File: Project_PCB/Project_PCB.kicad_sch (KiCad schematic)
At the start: 47 parts, among them J1 USB_C_2.0, J2 Myoware Connector, J3 Conn_01x02, SW1 RESET, SW2 BOOT, SW3 POWER, U1 ESP32-S3-WROOM-1, U2 RT9080-33GJ5, U3 MCP73831T-2ACI/OT, U4 LMV321

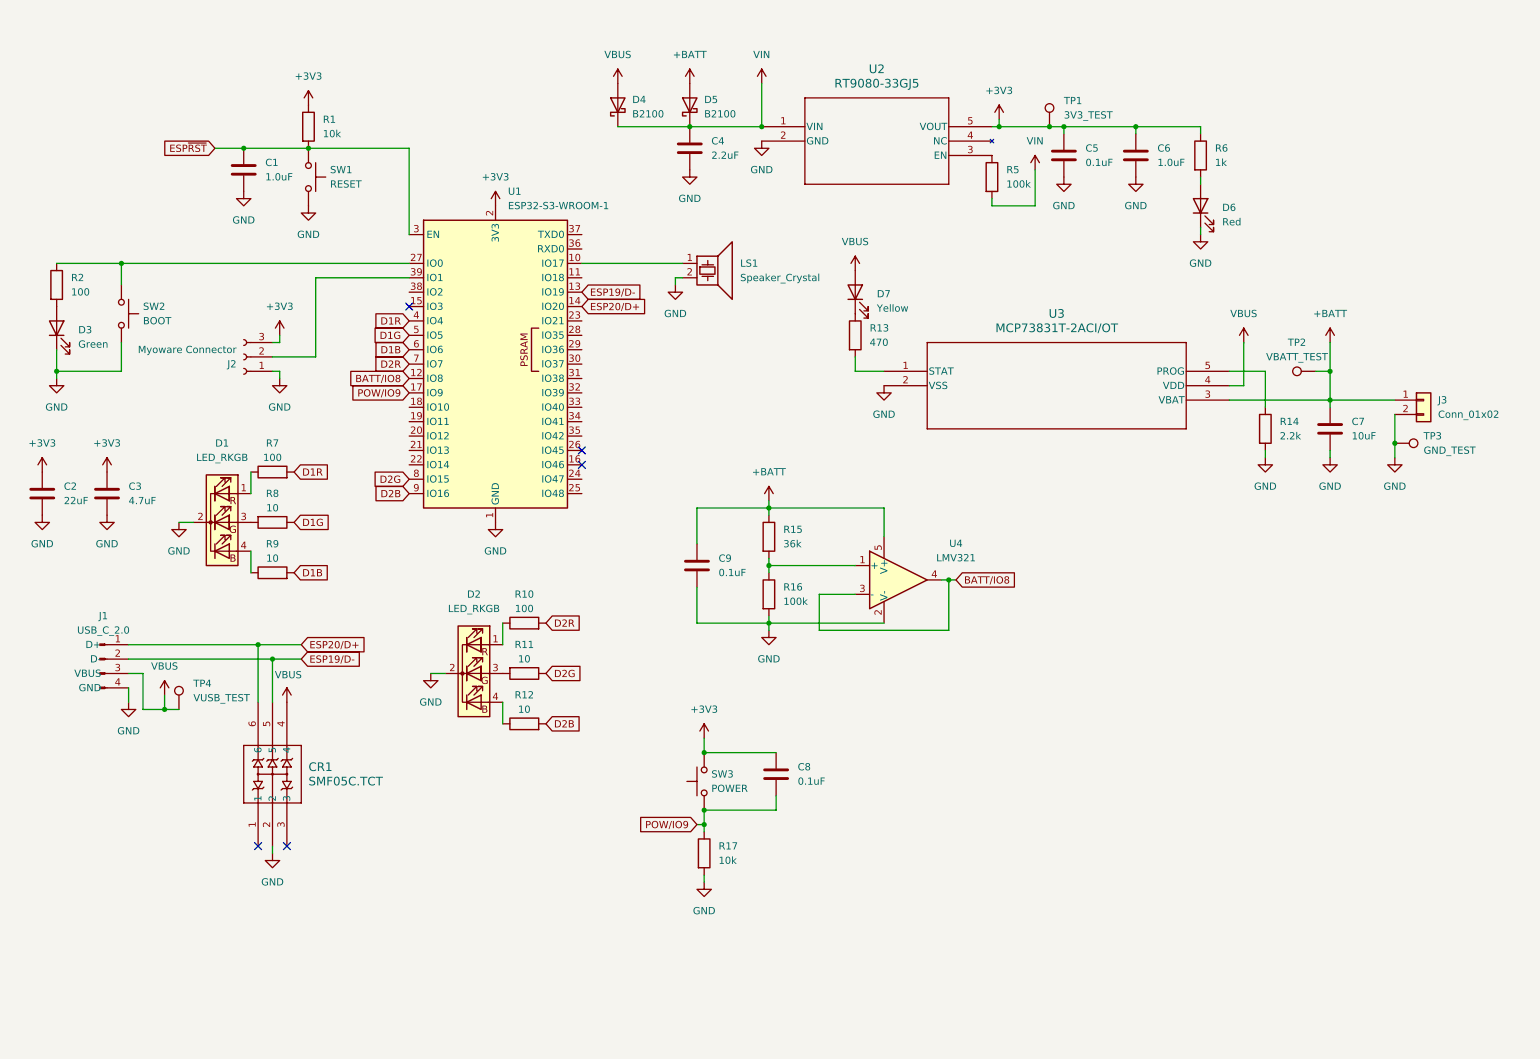
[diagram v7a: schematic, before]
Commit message: Made progress on PCB layout; minor changes in schematic to ease routing
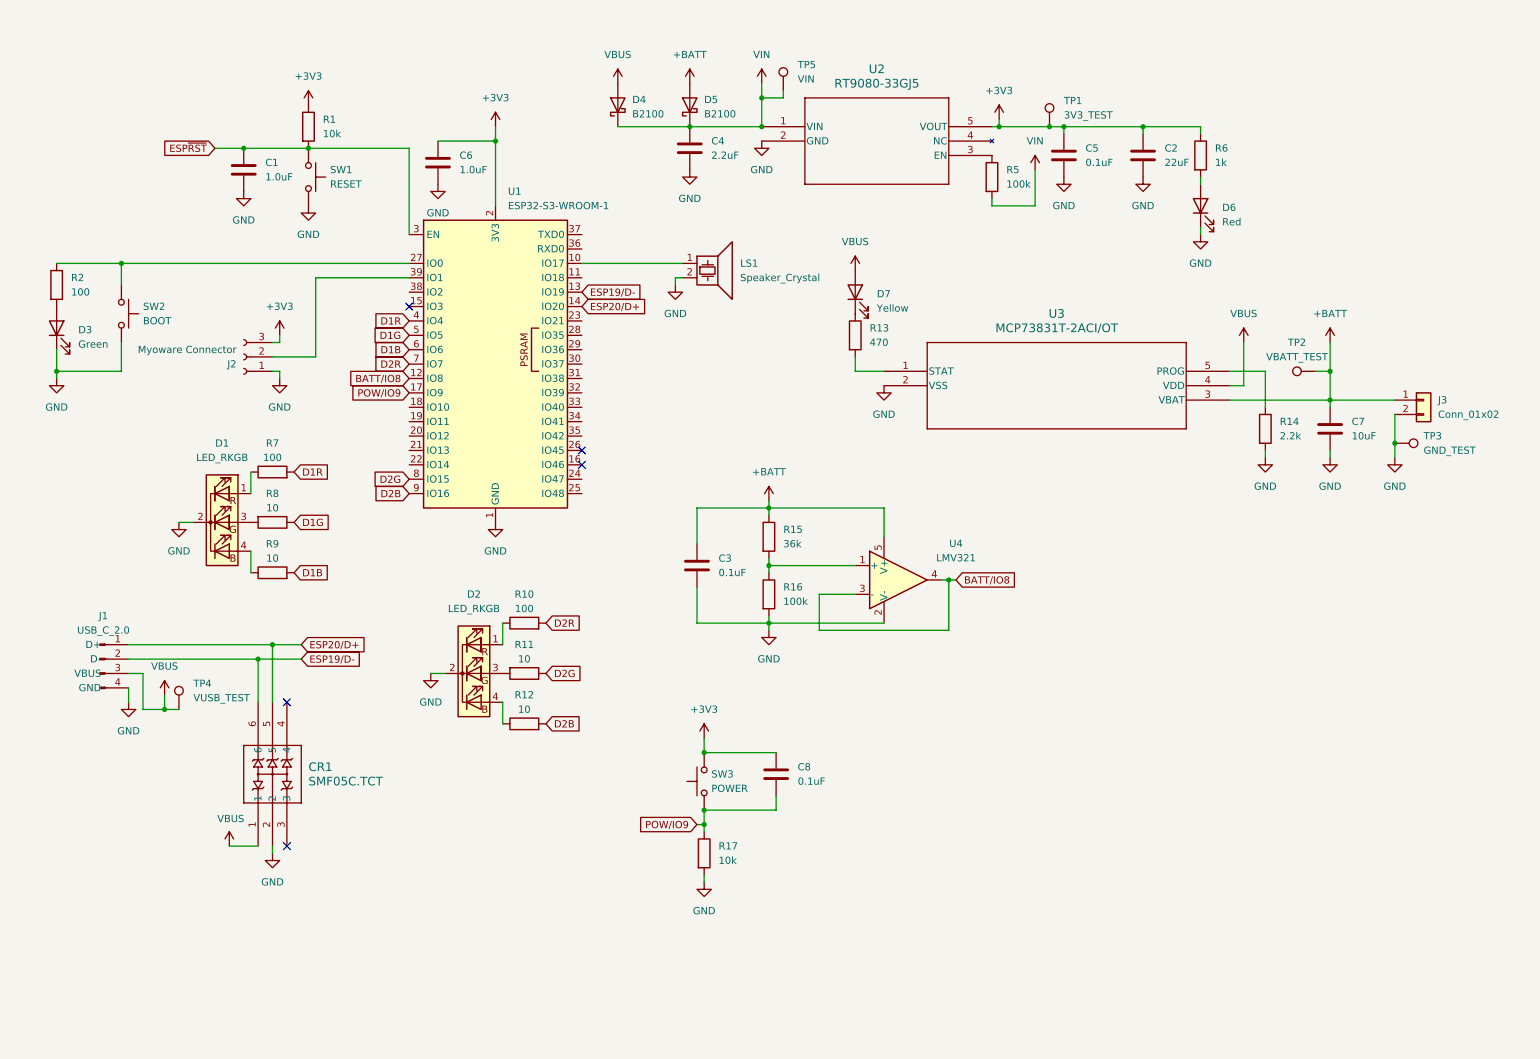
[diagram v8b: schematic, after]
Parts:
- removed C3: 4.7uF, Capacitor_THT:C_Radial_D5.0mm_H11.0mm_P2.00mm, symbol Device:C
- added TP5: VIN, TestPoint:TestPoint_THTPad_D2.0mm_Drill1.0mm, symbol Connector:TestPoint
- renumbered C9 to C3
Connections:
- net ESP19/D-: now also CR1.6; no longer CR1.5
- net ESP20/D+: now also CR1.5; no longer CR1.6
- net VBUS: now also CR1.1; no longer CR1.4
- net VIN: now also TP5.1
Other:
- moved on the sheet: C2, C6
